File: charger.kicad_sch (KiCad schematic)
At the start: 43 parts, among them J9 USB-C_CUI_UJC-HP-3-SMT-TR, Q14 SQS401EN-T1_BE3, U6 STUSB4500_QFN, U7 BQ25798RQMR

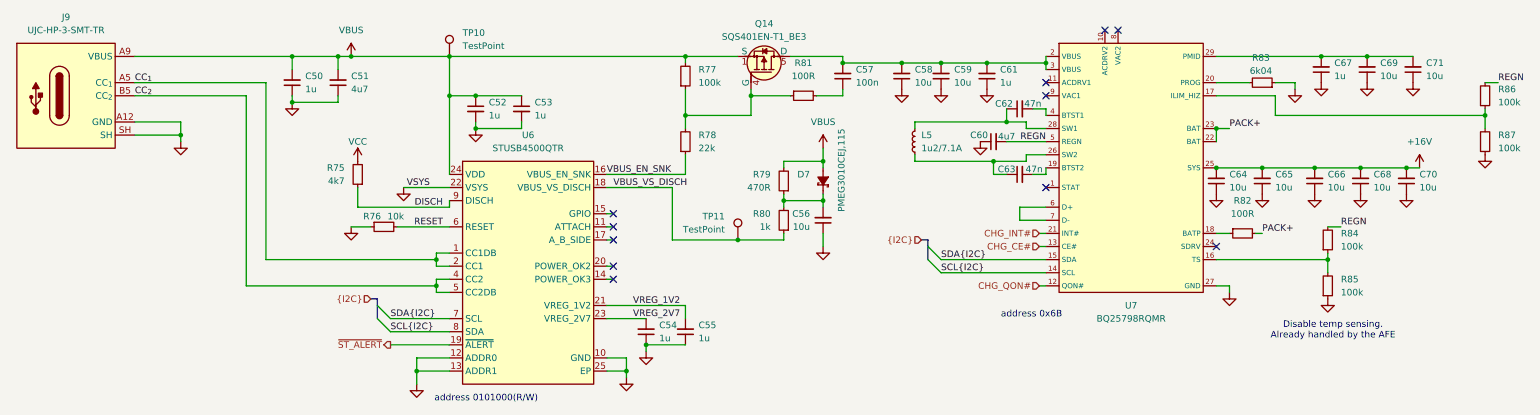
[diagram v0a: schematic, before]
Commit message: Minimal version without BMS
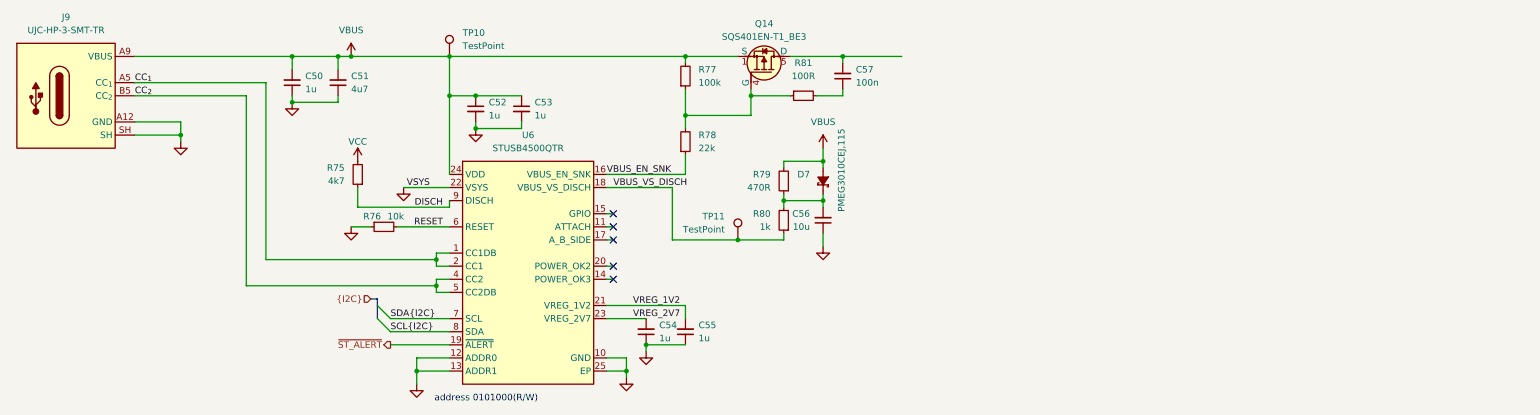
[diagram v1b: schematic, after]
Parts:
- removed C58, C59, C64, C65, C66, C68, C69, C70, C71: C_10u_10V_0402, Hardware Components Footprints:C_0402_1005Metric, symbol lib:C_10u_10V_0402
- removed C60: C_4u7_0805_50V, Hardware Components Footprints:C_0805_2012Metric, symbol lib:C_4u7_0805_50V
- removed C61, C67: C_1u_1210, Hardware Components Footprints:C_1210_3225Metric, symbol lib:C_1u_1210
- removed C62, C63: C_47n_0402, Hardware Components Footprints:C_0402_1005Metric, symbol lib:C_47n_0402
- removed L5: L_1u2_7.1A_Coilcraft-XFL4015, Hardware Components Footprints:L_Coilcraft-XFL4015, symbol lib:L_1u2_7.1A_Coilcraft-XFL4015
- removed R82: R_100R_0402, Hardware Components Footprints:R_0402_1005Metric, symbol lib:R_100R_0402
- removed R83: R_6k04_0.1%_0402, Hardware Components Footprints:R_0402_1005Metric, symbol lib:R_6k04_0.1%_0402
- removed R84, R85, R86, R87: R_100k_0.1%_0402, Hardware Components Footprints:R_0402_1005Metric, symbol lib:R_100k_0.1%_0402
- removed U7: BQ25798RQMR, jlc_footprints:QFN-29_L4.0-W4.0-P0.40-TL-BQ25792RQMR, symbol lib:BQ25798RQMR
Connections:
- no-connect marks 11 -> 5
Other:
- note removed: "Disable temp sensing. Already handled by the AFE"
- note removed: "address 0x6B"
